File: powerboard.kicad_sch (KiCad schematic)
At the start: 3 parts, among them J4 Conn_02x04, J5 Conn_02x04, J6 Conn_02x04

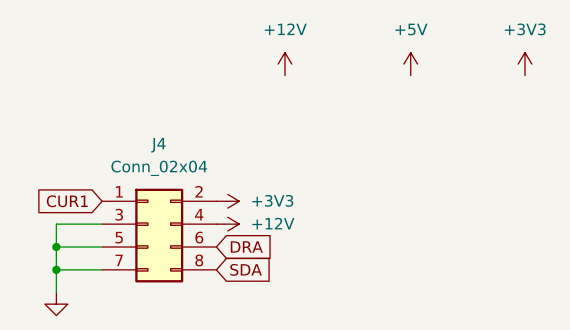
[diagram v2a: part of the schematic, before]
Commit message: Add files via upload
Add +12 and +5 outlets, change buzzer transistor, minor updates
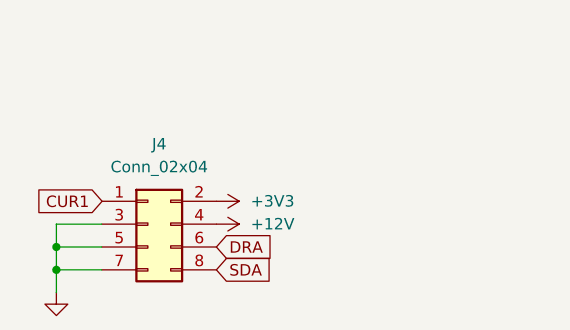
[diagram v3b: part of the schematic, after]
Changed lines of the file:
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@@
-    )
-  )
-  (symbol (lib_id "power:+5V") (at 175.26 24.13 0) (unit 1)
-    (in_bom yes) (on_board yes) (dnp no) (fields_autoplaced)
-    (property "Reference" "#PWR061" (at 175.26 27.94 0)
-      (effects (font (size 1.27 1.27)) hide)
-    )
-    (property "Value" "+5V" (at 175.26 19.05 0)
-      (effects (font (size 1.27 1.27)))
-    )
-    (property "Footprint" "" (at 175.26 24.13 0)
-      (effects (font (size 1.27 1.27)) hide)
-    )
-    (property "Datasheet" "" (at 175.26 24.13 0)
-      (effects (font (size 1.27 1.27)) hide)
-    )
-    (pin "1")
-    (instances
-      (project "ShiftWay_f103"
-        (path "/c57bc97c-1c43-4bb1-9424-fed846030b7b/0e47d56e-6599-490c-8484-306c0a411551"
-          (reference "#PWR061") (unit 1)
-        )
-      )
     )
   )
@@
     )
   )
-  (symbol (lib_id "PCM_4ms_Power-symbol:+12V") (at 161.29 24.13 0) (unit 1)
-    (in_bom yes) (on_board yes) (dnp no) (fields_autoplaced)
-    (property "Reference" "#PWR058" (at 161.29 27.94 0)
-      (effects (font (size 1.27 1.27)) hide)
-    )
-    (property "Value" "+12V" (at 161.29 19.05 0)
-      (effects (font (size 1.27 1.27)))
-    )
-    (property "Footprint" "" (at 161.29 24.13 0)
-      (effects (font (size 1.27 1.27)) hide)
-    )
-    (property "Datasheet" "" (at 161.29 24.13 0)
-      (effects (font (size 1.27 1.27)) hide)
-    )
-    (pin "1")
-    (instances
-      (project "ShiftWay_f103"
-        (path "/c57bc97c-1c43-4bb1-9424-fed846030b7b/0e47d56e-6599-490c-8484-306c0a411551"
-          (reference "#PWR058") (unit 1)
-        )
-      )
-    )
-  )
   (symbol (lib_id "PCM_4ms_Connector:Conn_02x04") (at 146.05 115.57 0) (unit 1)
     (in_bom yes) (on_board yes) (dnp no) (fields_autoplaced)
@@
         )
       )
-    )
-  )
-  (symbol (lib_id "power:+3V3") (at 187.96 24.13 0) (unit 1)
-    (in_bom yes) (on_board yes) (dnp no) (fields_autoplaced)
-    (property "Reference" "#PWR062" (at 187.96 27.94 0)
-      (effects (font (size 1.27 1.27)) hide)
-    )
-    (property "Value" "+3V3" (at 187.96 19.05 0)
-      (effects (font (size 1.27 1.27)))
-    )
-    (property "Footprint" "" (at 187.96 24.13 0)
-      (effects (font (size 1.27 1.27)) hide)
-    )
-    (property "Datasheet" "" (at 187.96 24.13 0)
-      (effects (font (size 1.27 1.27)) hide)
-    )
-    (pin "1")
-    (instances
-      (project "ShiftWay_f103"
-        (path "/c57bc97c-1c43-4bb1-9424-fed846030b7b/0e47d56e-6599-490c-8484-306c0a411551"
-          (reference "#PWR062") (unit 1)
-        )
-      )

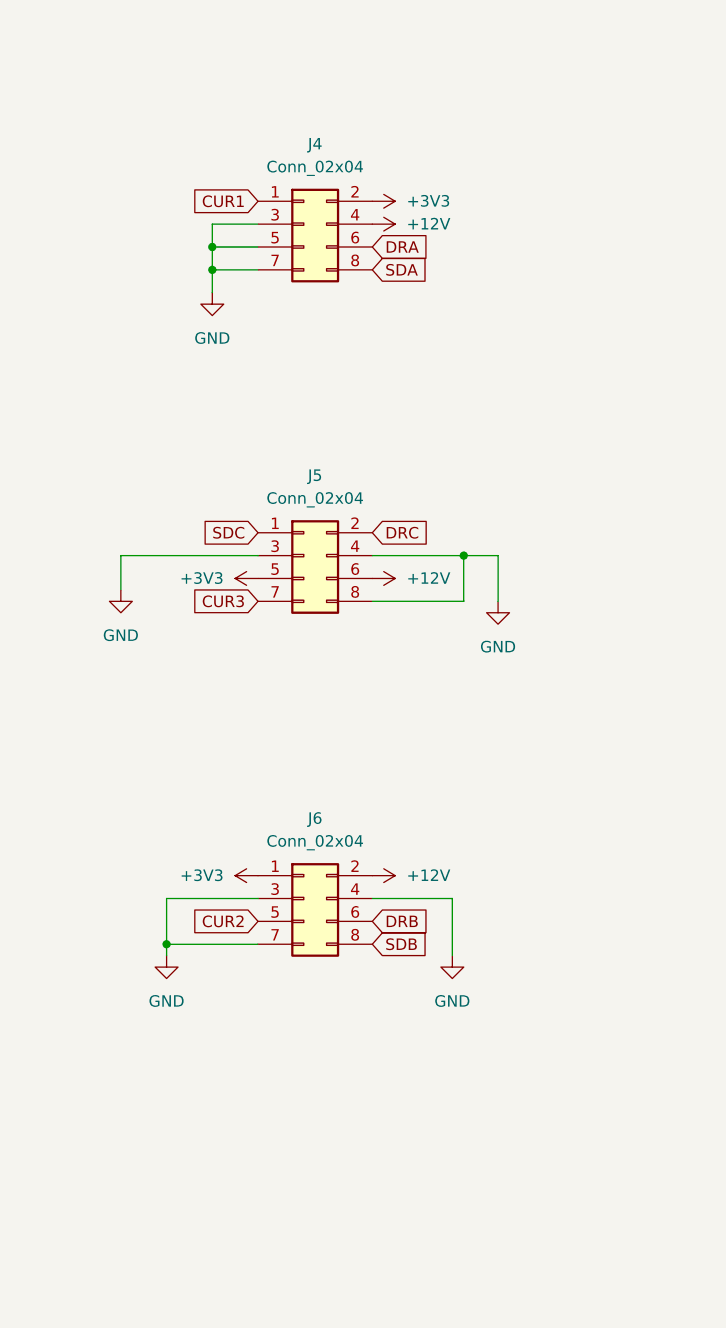
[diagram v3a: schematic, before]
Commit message: Divider, gate, mtr button, testpoints, minors
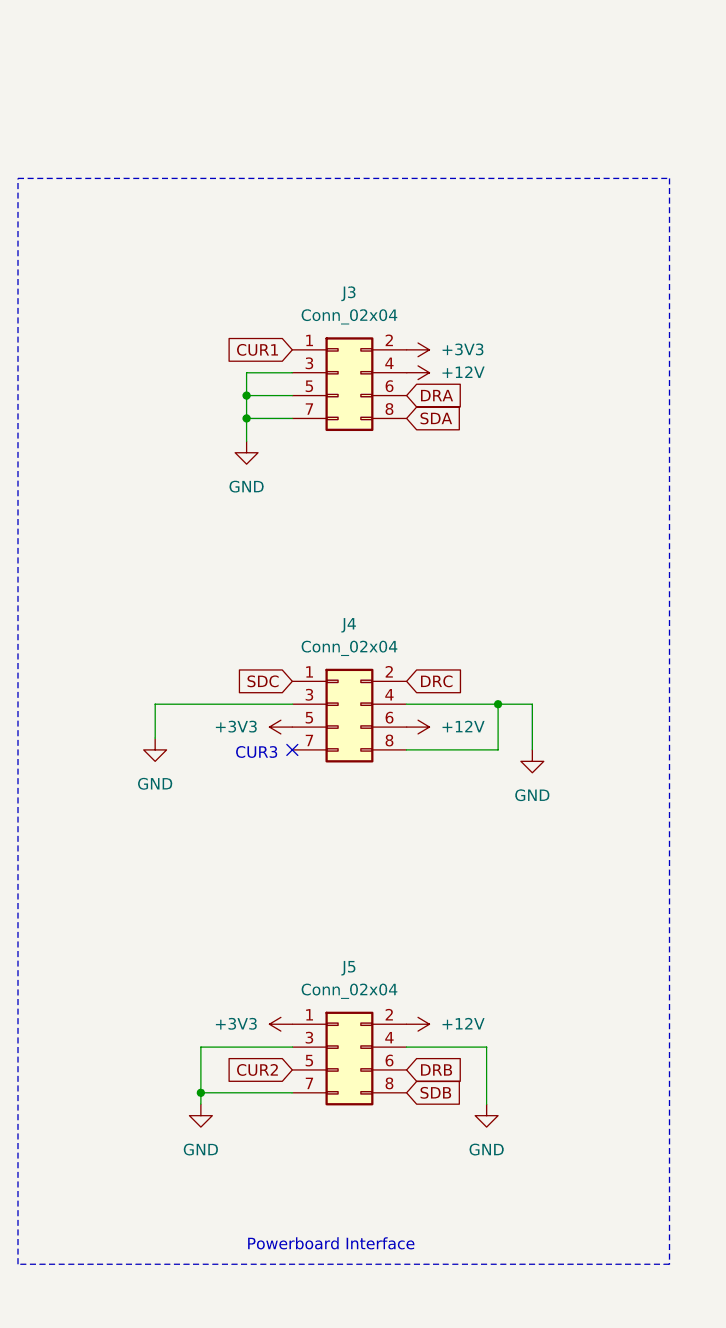
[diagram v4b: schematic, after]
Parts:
- renumbered J4 to J3, J5 to J4, J6 to J5
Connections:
- net CUR3: no longer names the net of J4.7 (Pin_7)
- no-connect marks 0 -> 1
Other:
- note added: "CUR3"
- note added: "Powerboard Interface"
- moved on the sheet: J3, J4, J5

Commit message: Minors, annotation
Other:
- title: (none) -> RedShift-117.6-LogicBoard-F103
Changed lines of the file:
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@@
 (kicad_sch (version 20230121) (generator eeschema)
   (paper "A4")
+  (title_block
+    (title "RedShift-117.6-LogicBoard-F103")
+    (date "08.12.2023")
+    (rev "0.1")
+  )
   (junction (at 139.7 62.23) (diameter 0) (color 0 0 0 0)
   )

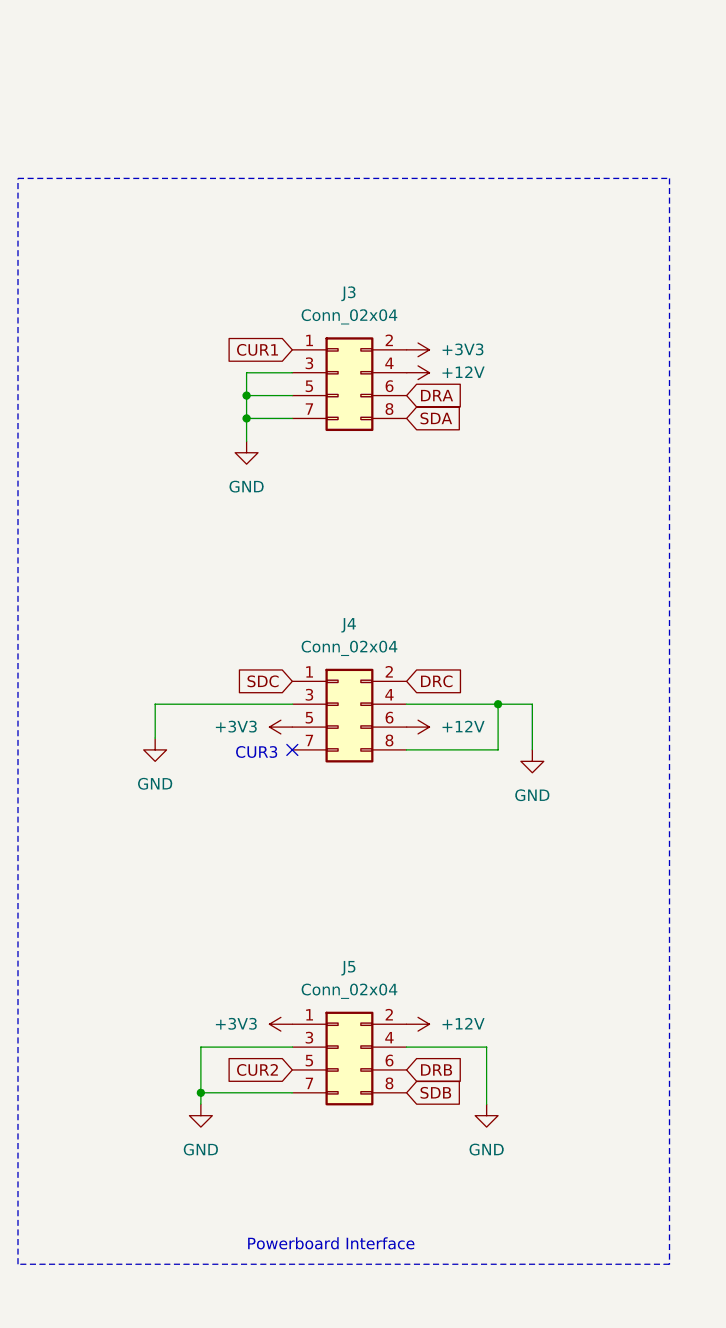
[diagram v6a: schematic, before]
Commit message: Add files via upload
Add leds and minors
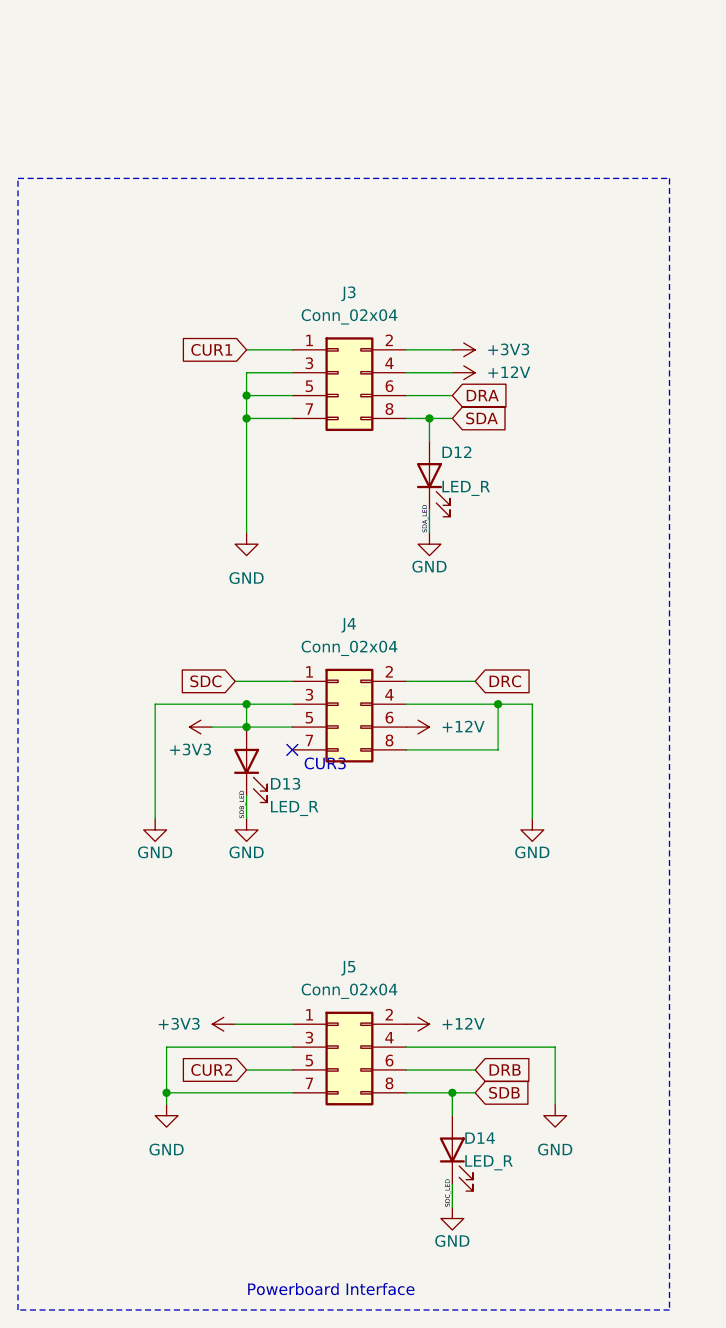
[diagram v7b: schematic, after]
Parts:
- added D12, D13, D14: LED_R, LED_SMD:LED_0603_1608Metric, symbol Device:LED
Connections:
- net GND is gone; now on net +3V3: J3.3 (Pin_3), J3.5 (Pin_5), J3.7 (Pin_7), J4.3 (Pin_3), J4.4 (Pin_4), J4.8 (Pin_8), J5.3 (Pin_3), J5.4 (Pin_4), J5.7 (Pin_7)
- net +3V3: now also D12.1 (K), D13.1 (K), D13.2 (A), D14.1 (K)
- net SDA: now also D12.2 (A)
- net SDB: now also D14.2 (A)

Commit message: fixed some footprints
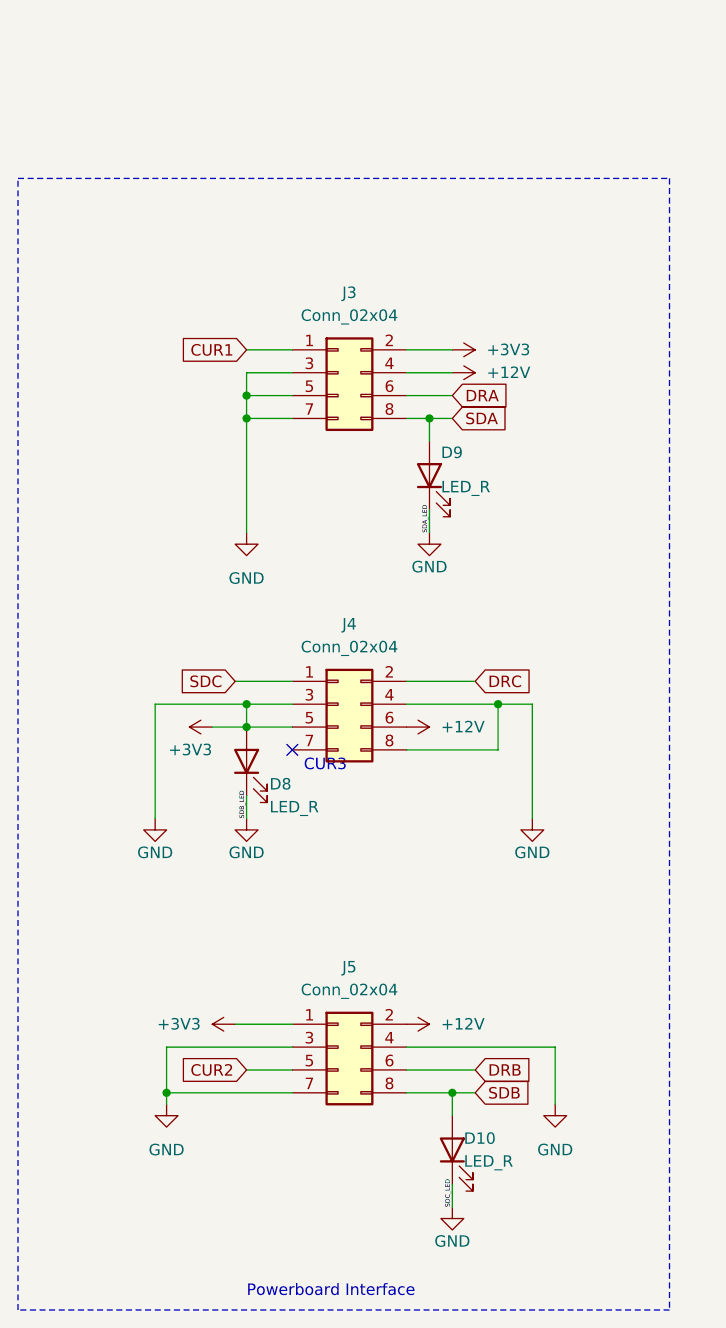
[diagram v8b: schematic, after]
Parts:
- J3, J4, J5: footprint 4ms_Connector:Pins_2x04_2.54mm_TH -> Connector_PinSocket_2.54mm:PinSocket_2x04_P2.54mm_Vertical
- renumbered D14 to D10, D13 to D8, D12 to D9
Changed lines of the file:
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@@
       (effects (font (size 1.27 1.27)))
     )
-    (property "Footprint" "4ms_Connector:Pins_2x04_2.54mm_TH" (at 153.035 107.95 0)
+    (property "Footprint" "Connector_PinSocket_2.54mm:PinSocket_2x04_P2.54mm_Vertical" (at 153.035 107.95 0)
       (effects (font (size 1.27 1.27)) hide)
     )
@@
       (effects (font (size 1.27 1.27)))
     )
-    (property "Footprint" "4ms_Connector:Pins_2x04_2.54mm_TH" (at 153.035 71.12 0)
+    (property "Footprint" "Connector_PinSocket_2.54mm:PinSocket_2x04_P2.54mm_Vertical" (at 153.035 71.12 0)
       (effects (font (size 1.27 1.27)) hide)
     )
@@
   (symbol (lib_id "PCM_4ms_Power-symbol:GND") (at 139.7 74.93 0) (unit 1)
     (in_bom yes) (on_board yes) (dnp no) (fields_autoplaced)
-    (property "Reference" "#PWR070" (at 139.7 81.28 0)
+    (property "Reference" "#PWR073" (at 139.7 81.28 0)
       (effects (font (size 1.27 1.27)) hide)
     )
@@
       (project "ShiftWay_f103"
         (path "/c57bc97c-1c43-4bb1-9424-fed846030b7b/0e47d56e-6599-490c-8484-306c0a411551"
-          (reference "#PWR070") (unit 1)
+          (reference "#PWR073") (unit 1)
         )
       )
@@
   (symbol (lib_id "PCM_4ms_Power-symbol:GND") (at 130.81 138.43 0) (unit 1)
     (in_bom yes) (on_board yes) (dnp no) (fields_autoplaced)
-    (property "Reference" "#PWR069" (at 130.81 144.78 0)
+    (property "Reference" "#PWR070" (at 130.81 144.78 0)
       (effects (font (size 1.27 1.27)) hide)
     )
@@
       (project "ShiftWay_f103"
         (path "/c57bc97c-1c43-4bb1-9424-fed846030b7b/0e47d56e-6599-490c-8484-306c0a411551"
-          (reference "#PWR069") (unit 1)
+          (reference "#PWR070") (unit 1)
         )
       )
@@
   (symbol (lib_id "PCM_4ms_Power-symbol:GND") (at 173.99 138.43 0) (unit 1)
     (in_bom yes) (on_board yes) (dnp no) (fields_autoplaced)
-    (property "Reference" "#PWR077" (at 173.99 144.78 0)
+    (property "Reference" "#PWR082" (at 173.99 144.78 0)
       (effects (font (size 1.27 1.27)) hide)
     )
@@
       (project "ShiftWay_f103"
         (path "/c57bc97c-1c43-4bb1-9424-fed846030b7b/0e47d56e-6599-490c-8484-306c0a411551"
-          (reference "#PWR077") (unit 1)
+          (reference "#PWR082") (unit 1)
         )
       )
@@
   (symbol (lib_id "PCM_4ms_Power-symbol:+12V") (at 162.56 57.15 270) (unit 1)
     (in_bom yes) (on_board yes) (dnp no) (fields_autoplaced)
-    (property "Reference" "#PWR074" (at 158.75 57.15 0)
+    (property "Reference" "#PWR079" (at 158.75 57.15 0)
       (effects (font (size 1.27 1.27)) hide)
     )
@@
       (project "ShiftWay_f103"
         (path "/c57bc97c-1c43-4bb1-9424-fed846030b7b/0e47d56e-6599-490c-8484-306c0a411551"
-          (reference "#PWR074") (unit 1)
+          (reference "#PWR079") (unit 1)
         )
       )
@@
   (symbol (lib_id "PCM_4ms_Power-symbol:GND") (at 171.45 106.68 0) (unit 1)
     (in_bom yes) (on_board yes) (dnp no)
-    (property "Reference" "#PWR078" (at 171.45 113.03 0)
+    (property "Reference" "#PWR081" (at 171.45 113.03 0)
       (effects (font (size 1.27 1.27)) hide)
     )
@@
       (project "ShiftWay_f103"
         (path "/c57bc97c-1c43-4bb1-9424-fed846030b7b/0e47d56e-6599-490c-8484-306c0a411551"
-          (reference "#PWR078") (unit 1)
+          (reference "#PWR081") (unit 1)
         )
       )
@@
   (symbol (lib_id "power:GND") (at 162.56 149.86 0) (unit 1)
     (in_bom yes) (on_board yes) (dnp no)
-    (property "Reference" "#PWR094" (at 162.56 156.21 0)
+    (property "Reference" "#PWR080" (at 162.56 156.21 0)
       (effects (font (size 1.27 1.27)) hide)
     )
@@
       (project "ShiftWay_f103"
         (path "/c57bc97c-1c43-4bb1-9424-fed846030b7b/0e47d56e-6599-490c-8484-306c0a411551"
-          (reference "#PWR094") (unit 1)
+          (reference "#PWR080") (unit 1)
         )
       )
@@
   (symbol (lib_id "Device:LED") (at 160.02 68.58 90) (unit 1)
     (in_bom yes) (on_board yes) (dnp no)
-    (property "Reference" "D12" (at 161.29 66.04 90)
+    (property "Reference" "D9" (at 161.29 66.04 90)
       (effects (font (size 1.27 1.27)) (justify right))
     )
@@
       (project "ShiftWay_f103"
         (path "/c57bc97c-1c43-4bb1-9424-fed846030b7b/0e47d56e-6599-490c-8484-306c0a411551"
-          (reference "D12") (unit 1)
+          (reference "D9") (unit 1)
         )
       )
@@
   (symbol (lib_id "power:GND") (at 160.02 74.93 0) (unit 1)
     (in_bom yes) (on_board yes) (dnp no)
-    (property "Reference" "#PWR092" (at 160.02 81.28 0)
+    (property "Reference" "#PWR077" (at 160.02 81.28 0)
       (effects (font (size 1.27 1.27)) hide)
     )
@@
       (project "ShiftWay_f103"
         (path "/c57bc97c-1c43-4bb1-9424-fed846030b7b/0e47d56e-6599-490c-8484-306c0a411551"
-          (reference "#PWR092") (unit 1)
+          (reference "#PWR077") (unit 1)
         )
       )
@@
   (symbol (lib_id "Device:LED") (at 162.56 143.51 90) (unit 1)
     (in_bom yes) (on_board yes) (dnp no)
-    (property "Reference" "D14" (at 163.83 142.24 90)
+    (property "Reference" "D10" (at 163.83 142.24 90)
       (effects (font (size 1.27 1.27)) (justify right))
     )
@@
       (project "ShiftWay_f103"
         (path "/c57bc97c-1c43-4bb1-9424-fed846030b7b/0e47d56e-6599-490c-8484-306c0a411551"
-          (reference "D14") (unit 1)
+          (reference "D10") (unit 1)
         )
       )
@@
   (symbol (lib_id "power:+3V3") (at 162.56 54.61 270) (unit 1)
     (in_bom yes) (on_board yes) (dnp no) (fields_autoplaced)
-    (property "Reference" "#PWR073" (at 158.75 54.61 0)
+    (property "Reference" "#PWR078" (at 158.75 54.61 0)
       (effects (font (size 1.27 1.27)) hide)
     )
@@
       (project "ShiftWay_f103"
         (path "/c57bc97c-1c43-4bb1-9424-fed846030b7b/0e47d56e-6599-490c-8484-306c0a411551"
-          (reference "#PWR073") (unit 1)
+          (reference "#PWR078") (unit 1)
         )
       )
@@
   (symbol (lib_id "PCM_4ms_Power-symbol:GND") (at 129.54 106.68 0) (unit 1)
     (in_bom yes) (on_board yes) (dnp no)
-    (property "Reference" "#PWR068" (at 129.54 113.03 0)
+    (property "Reference" "#PWR069" (at 129.54 113.03 0)
       (effects (font (size 1.27 1.27)) hide)
     )
@@
       (project "ShiftWay_f103"
         (path "/c57bc97c-1c43-4bb1-9424-fed846030b7b/0e47d56e-6599-490c-8484-306c0a411551"
-          (reference "#PWR068") (unit 1)
+          (reference "#PWR069") (unit 1)
         )
       )
@@
   (symbol (lib_id "power:GND") (at 139.7 106.68 0) (unit 1)
     (in_bom yes) (on_board yes) (dnp no)
-    (property "Reference" "#PWR093" (at 139.7 113.03 0)
+    (property "Reference" "#PWR074" (at 139.7 113.03 0)
       (effects (font (size 1.27 1.27)) hide)
     )
@@
       (project "ShiftWay_f103"
         (path "/c57bc97c-1c43-4bb1-9424-fed846030b7b/0e47d56e-6599-490c-8484-306c0a411551"
-          (reference "#PWR093") (unit 1)
+          (reference "#PWR074") (unit 1)
         )
       )
@@
       (effects (font (size 1.27 1.27)))
     )
-    (property "Footprint" "4ms_Connector:Pins_2x04_2.54mm_TH" (at 153.035 146.05 0)
+    (property "Footprint" "Connector_PinSocket_2.54mm:PinSocket_2x04_P2.54mm_Vertical" (at 153.035 146.05 0)
       (effects (font (size 1.27 1.27)) hide)
     )
@@
   (symbol (lib_id "Device:LED") (at 139.7 100.33 90) (unit 1)
     (in_bom yes) (on_board yes) (dnp no)
-    (property "Reference" "D13" (at 142.24 102.87 90)
+    (property "Reference" "D8" (at 142.24 102.87 90)
       (effects (font (size 1.27 1.27)) (justify right))
     )
@@
       (project "ShiftWay_f103"
         (path "/c57bc97c-1c43-4bb1-9424-fed846030b7b/0e47d56e-6599-490c-8484-306c0a411551"
-          (reference "D13") (unit 1)
-        )
-      )
+          (reference "D8") (unit 1)
+        )
+      )
